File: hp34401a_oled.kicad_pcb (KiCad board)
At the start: 2 copper layers, 30 x 33.5 mm, 35 parts, among them J1 USB_B_Micro, J2 DISPLAY, J3 UART, J4 FP, J5 DISPLAYPWR, U1 STM32F103C8Tx, U2 LM1117-3.3, U3 AT24C02, Y1 8M

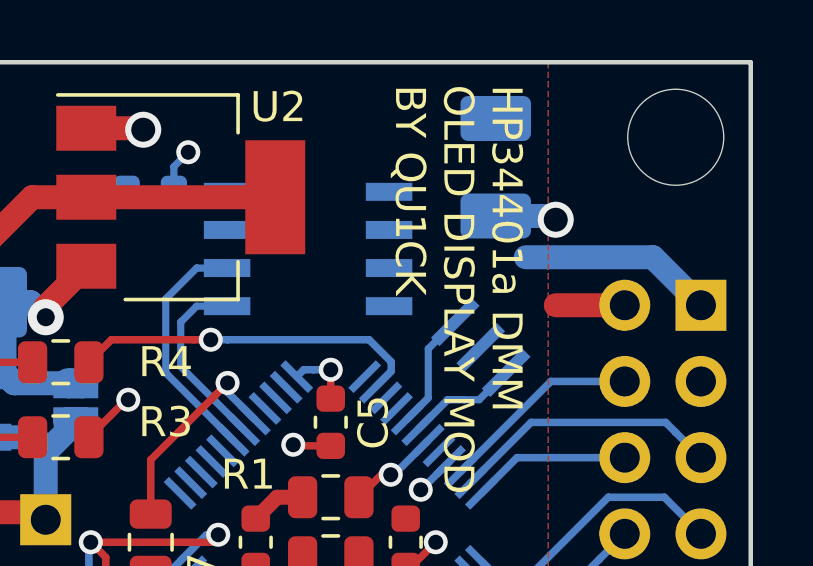
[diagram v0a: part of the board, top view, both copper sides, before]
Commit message: Small tweaks for KiCad 5.1 compatibility
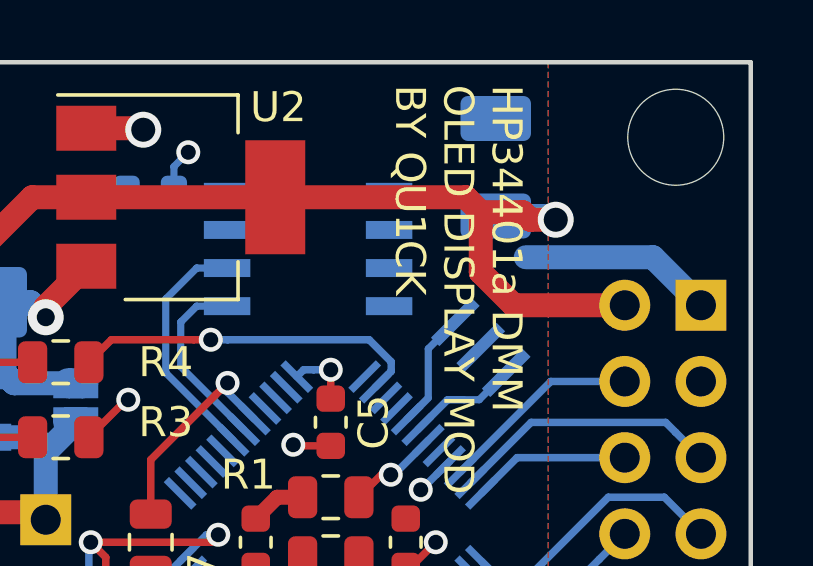
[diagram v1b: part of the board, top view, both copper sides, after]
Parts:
- REF**: value OSHW-Logo_5.7x6mm_SilkScreen -> OSHW-Logo
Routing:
- net +3V3: track 44.0 -> 58.6 mm
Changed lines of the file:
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@@
-(kicad_pcb (version 20171130) (host pcbnew "(5.0.0-rc3-dev-1-g99413bd05)")
+(kicad_pcb (version 20171130) (host pcbnew "(5.1.0)-1")
   (general
     (thickness 1.6)
     (drawings 21)
-    (tracks 244)
+    (tracks 251)
     (zones 0)
     (modules 35)
@@
     (zone_45_only no)
     (trace_min 0.24)
-    (segment_width 0.2)
-    (edge_width 0.15)
     (via_size 0.8)
     (via_drill 0.5)
@@
     (uvia_min_size 0.5)
     (uvia_min_drill 0.1)
+    (edge_width 0.15)
+    (segment_width 0.2)
     (pcb_text_width 0.3)
     (pcb_text_size 1.5 1.5)
@@
     (aux_axis_origin 0 0)
     (grid_origin 50 40)
-    (visible_elements 7FFFF7FF)
+    (visible_elements 7FFFFFFF)
     (pcbplotparams
       (layerselection 0x010f0_ffffffff)
@@
     (uvia_dia 0.5)
     (uvia_drill 0.3)
+    (diff_pair_width 0.3)
     (diff_pair_gap 0.25)
-    (diff_pair_width 0.3)
     (add_net +3V3)
     (add_net /BOOT0)
@@
     (uvia_dia 0.5)
     (uvia_drill 0.3)
+    (diff_pair_width 0.8)
     (diff_pair_gap 0.25)
-    (diff_pair_width 0.8)
     (add_net +12V)
     (add_net /Vin)
@@
     (uvia_dia 0.5)
     (uvia_drill 0.3)
+    (diff_pair_width 0.3)
     (diff_pair_gap 0.25)
-    (diff_pair_width 0.3)
     (add_net GND)
   )
@@
       (effects (font (size 1 1) (thickness 0.15)) (justify mirror))
     )
-    (fp_text value UART (at 0 -9.95 270) (layer B.Fab)
+    (fp_text value UART (at -2.5 -4.5) (layer B.Fab)
       (effects (font (size 1 1) (thickness 0.15)) (justify mirror))
     )
@@
       (effects (font (size 1 1) (thickness 0.15)) (justify mirror))
     )
-    (fp_text value FP (at 0 -15.03 270) (layer B.Fab)
+    (fp_text value FP (at -2 -6.5) (layer B.Fab)
       (effects (font (size 1 1) (thickness 0.15)) (justify mirror))
     )
@@
       (effects (font (size 1 1) (thickness 0.15)))
     )
-    (fp_text value 0.1uF (at 0 1.43 270) (layer F.Fab)
+    (fp_text value 0.1uF (at -2 1.43) (layer F.Fab)
       (effects (font (size 1 1) (thickness 0.15)))
     )
@@
       (effects (font (size 1 1) (thickness 0.15)))
     )
-    (fp_text value 0.1uF (at 0 1.43 90) (layer F.Fab)
+    (fp_text value 0.1uF (at -2 0 180) (layer F.Fab)
       (effects (font (size 1 1) (thickness 0.15)))
     )
@@
       (effects (font (size 1 1) (thickness 0.15)))
     )
-    (fp_text value 0.1uF (at 0 1.43 270) (layer F.Fab)
+    (fp_text value 0.1uF (at -2 0) (layer F.Fab)
       (effects (font (size 1 1) (thickness 0.15)))
     )
@@
       (effects (font (size 1 1) (thickness 0.15)))
     )
-    (fp_text value 0.1uF (at 0 1.43 270) (layer F.Fab)
+    (fp_text value 0.1uF (at 0 -3) (layer F.Fab)
       (effects (font (size 1 1) (thickness 0.15)))
     )
@@
       (effects (font (size 1 1) (thickness 0.15)))
     )
-    (fp_text value PWR (at 0 1.65 180) (layer F.Fab)
+    (fp_text value PWR (at 0 -2 180) (layer F.Fab)
       (effects (font (size 1 1) (thickness 0.15)))
     )
@@
       (effects (font (size 1 1) (thickness 0.15)) (justify mirror))
     )
-    (fp_text value BAT54C (at 0 -2.5 90) (layer B.Fab)
+    (fp_text value BAT54C (at -2 0 180) (layer B.Fab)
       (effects (font (size 1 1) (thickness 0.15)) (justify mirror))
     )
@@
       (effects (font (size 1 1) (thickness 0.15)))
     )
-    (fp_text value BOOT (at 0 1.9 90) (layer F.Fab)
+    (fp_text value BOOT (at -0.75 0 90) (layer F.Fab)
       (effects (font (size 1 1) (thickness 0.15)))
     )
@@
       (effects (font (size 1 1) (thickness 0.15)) (justify mirror))
     )
-    (fp_text value "NO DIODE" (at 0 -1.9 90) (layer B.Fab)
+    (fp_text value "NO DIODE" (at 0 -1.9 90) (layer B.Fab) hide
       (effects (font (size 1 1) (thickness 0.15)) (justify mirror))
     )
@@
       (effects (font (size 1 1) (thickness 0.15)))
     )
-    (fp_text value 100k (at 0 1.65) (layer F.Fab)
+    (fp_text value 100k (at 3.5 -1) (layer F.Fab)
       (effects (font (size 1 1) (thickness 0.15)))
     )
@@
       (effects (font (size 1 1) (thickness 0.15)) (justify mirror))
     )
-    (fp_text value 1K5 (at 0 -1.65) (layer B.Fab)
+    (fp_text value 1K5 (at -3 0) (layer B.Fab)
       (effects (font (size 1 1) (thickness 0.15)) (justify mirror))
     )
@@
       (effects (font (size 1 1) (thickness 0.15)))
     )
-    (fp_text value 1K (at 0 1.65) (layer F.Fab)
+    (fp_text value 1K (at 2.5 0) (layer F.Fab)
       (effects (font (size 1 1) (thickness 0.15)))
     )
@@
       (effects (font (size 1 1) (thickness 0.15)))
     )
-    (fp_text value 1K (at 0 1.65) (layer F.Fab)
+    (fp_text value 1K (at 2.5 0) (layer F.Fab)
       (effects (font (size 1 1) (thickness 0.15)))
     )
@@
       (effects (font (size 1 1) (thickness 0.15)) (justify mirror))
     )
-    (fp_text value 22R (at 0 -1.65 180) (layer B.Fab)
+    (fp_text value 22R (at 3 0 180) (layer B.Fab)
       (effects (font (size 1 1) (thickness 0.15)) (justify mirror))
     )
@@
       (effects (font (size 1 1) (thickness 0.15)) (justify mirror))
     )
-    (fp_text value 22R (at 0 -1.65 180) (layer B.Fab)
+    (fp_text value 22R (at 3 0 180) (layer B.Fab)
       (effects (font (size 1 1) (thickness 0.15)) (justify mirror))
     )
@@
       (effects (font (size 1 1) (thickness 0.15)))
     )
-    (fp_text value 100k (at 0 1.65 90) (layer F.Fab)
+    (fp_text value 100k (at -2 0 180) (layer F.Fab)
       (effects (font (size 1 1) (thickness 0.15)))
     )
@@
       (effects (font (size 1 1) (thickness 0.15)))
     )
-    (fp_text value 100k (at 0 1.65) (layer F.Fab)
+    (fp_text value 100k (at 3.5 1.65) (layer F.Fab)
       (effects (font (size 1 1) (thickness 0.15)))
     )
@@
       (effects (font (size 1 1) (thickness 0.15)))
     )
-    (fp_text value LM1117-3.3 (at 0 4.5) (layer F.Fab)
+    (fp_text value LM1117-3.3 (at 7 0) (layer F.Fab)
       (effects (font (size 1 1) (thickness 0.15)))
     )
@@
       (effects (font (size 1 1) (thickness 0.15)))
     )
-    (fp_text value MountingHole (at 0 3.75) (layer F.Fab)
+    (fp_text value MountingHole (at -8 0) (layer F.Fab) hide
       (effects (font (size 1 1) (thickness 0.15)))
     )
@@
       (effects (font (size 1 1) (thickness 0.15)))
     )
-    (fp_text value MountingHole (at 0 3.75) (layer F.Fab)
+    (fp_text value MountingHole (at 8.5 0) (layer F.Fab) hide
       (effects (font (size 1 1) (thickness 0.15)))
     )
@@
       (effects (font (size 1 1) (thickness 0.15)))
     )
-    (fp_text value MountingHole (at 0 3.75) (layer F.Fab)
+    (fp_text value MountingHole (at 8.5 0) (layer F.Fab) hide
       (effects (font (size 1 1) (thickness 0.15)))
     )
@@
       (effects (font (size 1 1) (thickness 0.15)))
     )
-    (fp_text value MountingHole (at 0 3.75) (layer F.Fab)
+    (fp_text value MountingHole (at -8 0) (layer F.Fab) hide
       (effects (font (size 1 1) (thickness 0.15)))
     )
@@
       (effects (font (size 1 1) (thickness 0.15)) (justify mirror))
     )
-    (fp_text value 47uF (at 0 -2.35 180) (layer B.Fab)
+    (fp_text value 47uF (at -4 0 180) (layer B.Fab)
       (effects (font (size 1 1) (thickness 0.15)) (justify mirror))
     )
@@
       (effects (font (size 1 1) (thickness 0.15)) (justify mirror))
     )
-    (fp_text value 47uF (at 0 -2.35 90) (layer B.Fab)
+    (fp_text value 47uF (at 0 3.5 180) (layer B.Fab)
       (effects (font (size 1 1) (thickness 0.15)) (justify mirror))
     )
@@
       (effects (font (size 1 1) (thickness 0.15)) (justify mirror))
     )
-    (fp_text value 10K (at 0 -2.8 90) (layer B.Fab)
+    (fp_text value 10K (at 0 3.5 180) (layer B.Fab)
       (effects (font (size 1 1) (thickness 0.15)) (justify mirror))
     )
@@
       (effects (font (size 1 1) (thickness 0.15)))
     )
-    (fp_text value OSHW-Logo_5.7x6mm_SilkScreen (at 0.75 0) (layer F.Fab) hide
+    (fp_text value OSHW-Logo (at 0.75 0) (layer F.Fab) hide
       (effects (font (size 1 1) (thickness 0.15)))
     )
@@
   (segment (start 71.5 45.125) (end 73.375 45.125) (width 0.8) (layer B.Cu) (net 2))
   (segment (start 73.375 45.125) (end 73.5 45.25) (width 0.8) (layer B.Cu) (net 2))
-  (segment (start 73.5 48.1) (end 75.8 48.1) (width 0.8) (layer F.Cu) (net 2))
+  (segment (start 70.5 44.5) (end 64.15 44.5) (width 0.8) (layer F.Cu) (net 2))
+  (segment (start 71 45) (end 70.5 44.5) (width 0.8) (layer F.Cu) (net 2))
+  (segment (start 71 47) (end 71 45) (width 0.8) (layer F.Cu) (net 2))
+  (segment (start 75.8 48.1) (end 72.1 48.1) (width 0.8) (layer F.Cu) (net 2))
+  (segment (start 72.1 48.1) (end 71 47) (width 0.8) (layer F.Cu) (net 2))
+  (segment (start 72.401472 45) (end 71 45) (width 0.8) (layer F.Cu) (net 2))
+  (segment (start 72.651472 45.25) (end 72.401472 45) (width 0.8) (layer F.Cu) (net 2))
+  (segment (start 73.5 45.25) (end 72.651472 45.25) (width 0.8) (layer F.Cu) (net 2))
   (segment (start 56.0625 52.5) (end 53.9375 52.5) (width 0.25) (layer F.Cu) (net 3))
   (segment (start 56.0625 50) (end 53.9375 50) (width 0.25) (layer F.Cu) (net 4))
@@
   (zone (net 2) (net_name +3V3) (layer F.Cu) (hatch edge 0.508)
     (connect_pads (clearance 0.24))
-    (min_thickness 0.25)
+    (min_thickness 0.24)
     (fill yes (arc_segments 16) (thermal_gap 0.508) (thermal_bridge_width 0.508))
     (polygon
@@
   (zone (net 1) (net_name GND) (layer B.Cu) (hatch edge 0.508)
     (connect_pads (clearance 0.24))
-    (min_thickness 0.25)
+    (min_thickness 0.24)
     (fill yes (arc_segments 16) (thermal_gap 0.508) (thermal_bridge_width 0.508))
     (polygon
